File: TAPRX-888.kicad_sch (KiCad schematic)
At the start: 126 parts, among them J1 CONN_SMA_JACK_EDGE_JLC_With_N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, J11 Conn_JTAG10-mini, J2 CONN_SMA_JACK_EDGE_JLC_With_N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, J3 CONN_SMA_JACK_EDGE_JLC_With_N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, J4 CONN_SMA_JACK_EDGE_JLC_With_N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, J5 USB-3.0, U1 AP2114H-3.3TRG1, U10 XO-19.2MHZ, U11 CYUSB3014-BZXCT, U2 AP2114H-3.3TRG1, U3 AP2114H-3.3TRG1, U4 LP5907MFX-3.3, U5 UMW AMS1117-1.2, U6 AD8370, U7 TVS-SP3011, U8 LTC2208CUP#PBF, U9 MX25L3233FM2I

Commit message: Bring over ringof/dev (tranche 2, stage 1): design, library, 3D, board CI & docs
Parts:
- B1: footprint TIS_Footprints:BUTTON-4p5X4p5 -> Library:BUTTON-4p5X4p5
- C1, C10, C15, C16, C17, C18, C19, C2, C20, C21, C23, C24, C26, C27, C28, C3, C30, C31, C32, C34, C35, C36, C37, C38, C39, C40, C42, C43, C44, C46, C5, C6, C7, C77, C8, C9: footprint TIS_Footprints:C_0603 -> Library:C_0603
- C11, C12, C13, C14, C22, C25, C29, C4, C41, C45, C47: footprint TIS_Footprints:PAD_0603 -> Library:C_0603
- C33: footprint TIS_Footprints:PAD_1206 -> Library:PAD_1206
- D1, D2: footprint TIS_Footprints:SOD-123 -> Library:SOD-123
- D3: footprint TIS_Footprints:LED_RGB_SIDE -> Library:LED_RGB_SIDE
- H1, H2, H3, H4: footprint TIS_Footprints:MountingHole_M2.5-PTH -> Library:MountingHole_M2.5-PTH
- J1, J2, J3, J4: footprint TIS_Footprints:SMA_Jack_EdgeMount_JLC_With_Nut -> Library:SMA_Jack_EdgeMount_JLC_With_Nut; symbol TIS:CONN_SMA_JACK_EDGE_JLC_with_nut -> Library:CONN_SMA_JACK_EDGE_JLC_with_nut
- J11: footprint TIS_Footprints:CONN-JTAG10-mini -> Library:CONN-JTAG10-mini
- J5: footprint TIS_Footprints:USB-3.0 -> Library:USB-3.0
- L1, L3, L4, L5, L6, L7: footprint TIS_Footprints:0603 -> Library:0603
- L2: footprint TIS_Footprints:TIS-Logo -> Library:TIS-Logo
- R1, R13, R14, R15, R16, R17, R18, R19, R2, R20, R21, R22, R23, R24, R25, R26, R27, R3, R4, R5, R58, R59, R6, R7, R8: footprint TIS_Footprints:PAD_0603 -> Library:PAD_0603
- R10, R11, R12, R9: footprint TIS_Footprints:4D02 -> Library:4D02
- TP1, TP10, TP11, TP12, TP13, TP14, TP2, TP3, TP4, TP5, TP6, TP7, TP8, TP9: footprint TIS_Footprints:TP -> Library:TP; now not fitted
- TP20: footprint TIS_Footprints:TP-Tiny -> Library:TP-Tiny; now not fitted
- TP21: footprint TIS_Footprints:TP-Tiny -> Library:TP-Tiny; now not fitted; now left out of the parts list
- U1, U2, U3, U5: footprint TIS_Footprints:SOT-223_THERMAL -> Library:SOT-223_THERMAL
- U10: footprint TIS_Footprints:SMD-2520 -> Library:SMD-2520
- U11: footprint TIS_Footprints:BGA-121 -> Library:BGA-121
- U4: footprint TIS_Footprints:SOT-23-5 -> Library:SOT-23-5
- U6: footprint TIS_Footprints:TSSOP-16-Thermal -> Library:TSSOP-16-Thermal
- U7: footprint TIS_Footprints:SP3011 -> Library:SP3011
- U8: footprint TIS_Footprints:QFN-64_EP_9.5x9.5_Pitch0.5mm -> Library:QFN-64_EP_9.5x9.5_Pitch0.5mm
- U9: footprint TIS_Footprints:SOIC-8-dual -> Library:SOIC-8-dual
- Z1: footprint TIS_Footprints:SOD-323 -> Library:SOD-323

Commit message: fix BAV99 value, TIS exclude from BOM
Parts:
- L2: now left out of the parts list
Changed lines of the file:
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@@
 		(body_style 1)
 		(exclude_from_sim no)
-		(in_bom yes)
+		(in_bom no)
 		(on_board yes)
 		(in_pos_files yes)

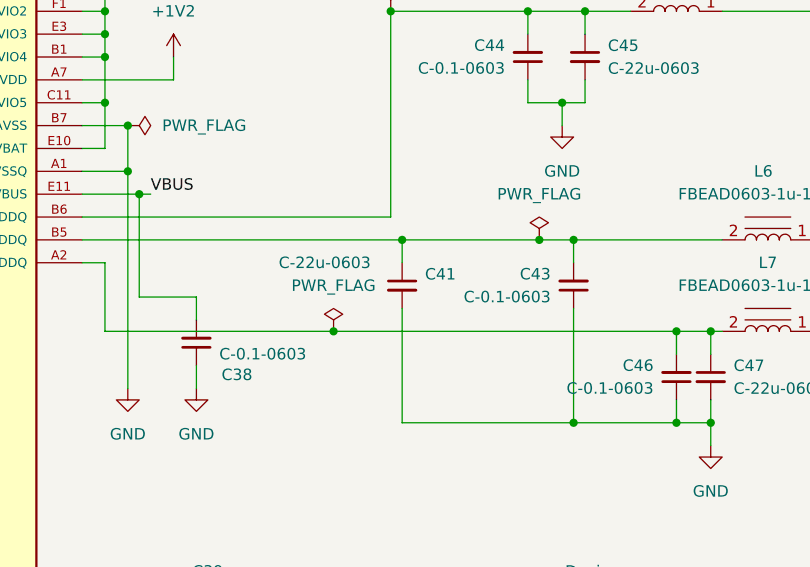
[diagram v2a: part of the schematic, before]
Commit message: Reconcile library/schematic/board drift (ERC/DRC clean at full severity)
Full-severity ERC/DRC surfaced 22 lib_symbol_mismatch + 5 lib_footprint_mismatch
warnings from cached copies drifting off the library master. Reconciled and
verified against the schematic and board:

- Symbol caches: refresh 8 cap/diode symbols whose embedded footprint field was
  stale (PAD_0603 -> C_0603); instances and PCB already used C_0603.
- SMA (J1-J4): push the board's tuned 3D-model offset/rotate into the library
  master and re-save it in KiCad 10 format; fix J1 LCSC C2874826 -> C914558 in
  schematic and board (J1 was an error, not a variant).
- U.FL (J10): re-save library footprint in v10 to match the routed board.

Result: ERC 0, DRC 0 (errors + warnings).
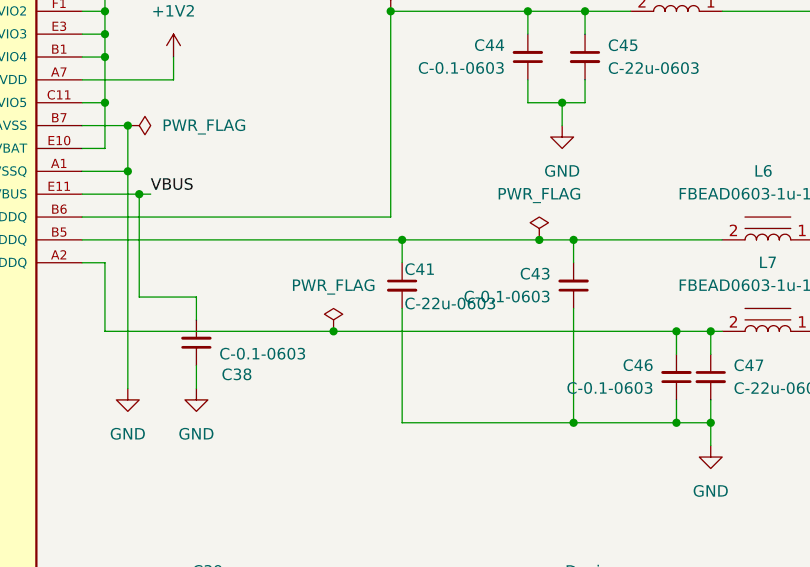
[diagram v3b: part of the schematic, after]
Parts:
- J1: LCSC Part # C2874826 -> C914558
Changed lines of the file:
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@@
 			)
 		)
-		(property "LCSC Part #" "C2874826"
+		(property "LCSC Part #" "C914558"
 			(at 30.226 11.43 0)
 			(hide yes)
@@
 		)
 		(property "Footprint" "Library:C_0603"
-			(at 119.634 108.712 0)
+			(at 135.636 105.664 0)
 			(hide yes)
 			(show_name no)
@@
 		)
 		(property "Description" "1uF 50V X5R 0603"
-			(at 121.92 107.95 0)
+			(at 133.096 107.696 0)
 			(hide yes)
 			(show_name no)
@@
 		)
 		(property "LCSC Part #" "C15849"
-			(at 121.92 107.95 0)
+			(at 130.048 103.632 0)
 			(hide yes)
 			(show_name no)
@@
 		(dnp no)
 		(property "Reference" "C41"
-			(at 349.25 92.7162 0)
+			(at 346.964 92.202 0)
 			(show_name no)
 			(do_not_autoplace no)
@@
 		)
 		(property "Value" "C-22u-0603"
-			(at 332.994 91.44 0)
-			(show_name no)
-			(do_not_autoplace no)
+			(at 346.964 96.012 0)
+			(show_name no)
+			(do_not_autoplace no)
